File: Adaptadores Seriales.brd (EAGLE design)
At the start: 141.2 x 32.3 mm, 18 parts, among them X13 22-23-2031, X14 22-23-2031, X15 22-23-2031, X16 22-23-2031, X17 22-23-2031, X18 22-23-2031

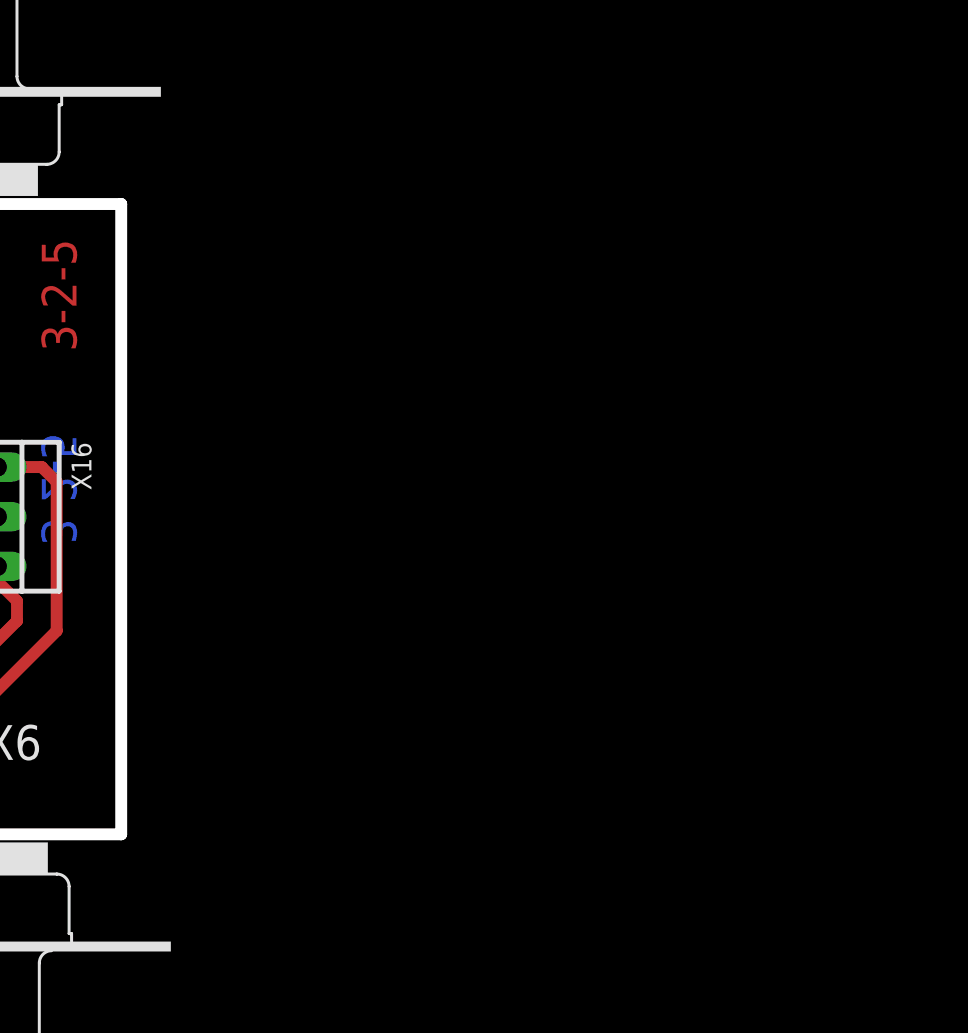
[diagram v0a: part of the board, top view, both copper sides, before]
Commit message: Añadido Conversor MAX-232, con pine de 3v3 para Raspberry
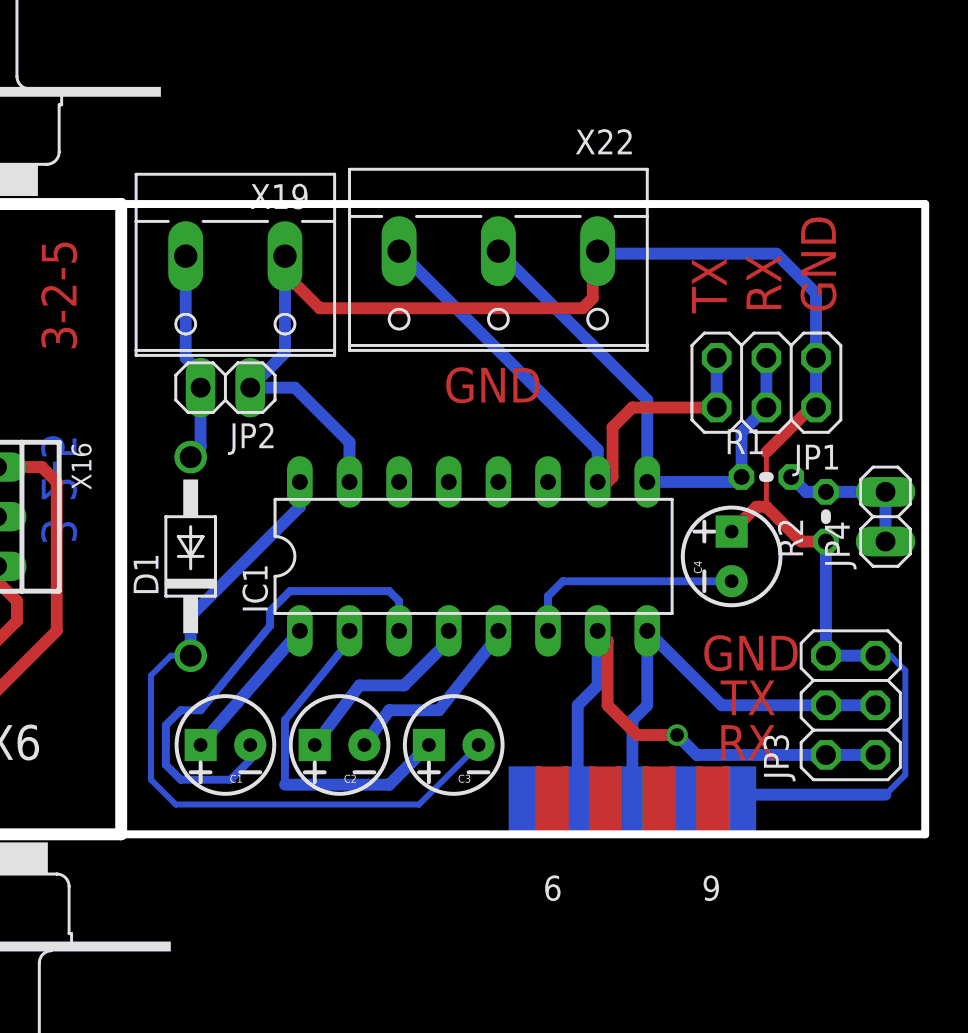
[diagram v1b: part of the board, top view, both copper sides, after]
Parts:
- added C1, C2, C3, C4: (no value), SparkFun-Capacitors:CPOL-RADIAL-10UF-25V-KIT
- added D1: 1N4004, diode:DO41-10
- added IC1: MAX232, maxim:DIL16
- added JP1, JP3: (no value), pinhead:2X03
- added JP2, JP4: (no value), pinhead:1X02
- added R1: 1K, rcl:0204V
- added R2: 2K, rcl:0204V
- added X19: (no value), con-wago-508:W237-132
- added X20: (no value), con-subd:F09D
- added X22: (no value), con-wago-508:W237-133
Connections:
- new net GND_1: C4.1, IC1.15, JP1.1, JP1.2, JP2.1, JP3.5, JP3.6, R2.1, X19.1, X20.5, X22.1
- new net N$1: C1.1, IC1.1
- new net N$10: C4.2, IC1.6
- new net N$13: JP4.1, JP4.2, R1.2, R2.2
- new net N$4: C1.2, IC1.3
- new net N$6: D1.A, JP2.2, X19.2
- new net N$7: C2.1, IC1.4
- new net N$8: C2.2, IC1.5
- new net N$9: C3.1, IC1.2
- new net PIN2-1: IC1.14
- new net PIN2_2: IC1.7, JP3.1, JP3.2, X20.2
- new net PIN3_1: IC1.13
- new net PIN3_2: IC1.8, JP3.3, JP3.4, X20.3
- new net RX1_TTL: IC1.12
- new net RX2_TTL: IC1.9, JP1.3, JP1.4, R1.1, X22.2
- new net TX1_TTL: IC1.11
- new net TX2_TTL: IC1.10, JP1.5, JP1.6, X22.3
- new net VCC_1: C3.2, D1.C, IC1.16
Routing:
- net GND_1: track 0.00 -> 90.7 mm
- net VCC_1: track 0.00 -> 37.5 mm
- net PIN2_2: track 0.00 -> 27.9 mm, vias 0 -> 1
- net TX2_TTL: track 0.00 -> 27.7 mm
- net RX2_TTL: track 0.00 -> 26.5 mm
- net N$4: track 0.00 -> 25.1 mm
- net PIN3_2: track 0.00 -> 22.3 mm
- net N$9: track 0.00 -> 17.3 mm
- net N$10: track 0.00 -> 11.5 mm
- net N$6: track 0.00 -> 10.8 mm
- net N$8: track 0.00 -> 9.86 mm
- net N$7: track 0.00 -> 9.84 mm
- net N$1: track 0.00 -> 7.74 mm
- net N$13: track 0.00 -> 7.68 mm
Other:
- board size 141.2 x 32.3 mm -> 182.4 x 32.3 mm
- board text added: "GND"
- board text added: "RX"
- board text added: "TX"
